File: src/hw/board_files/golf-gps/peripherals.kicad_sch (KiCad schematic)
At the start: 15 parts, among them J2 Micro_SD_Card, U1 NEO-M9N

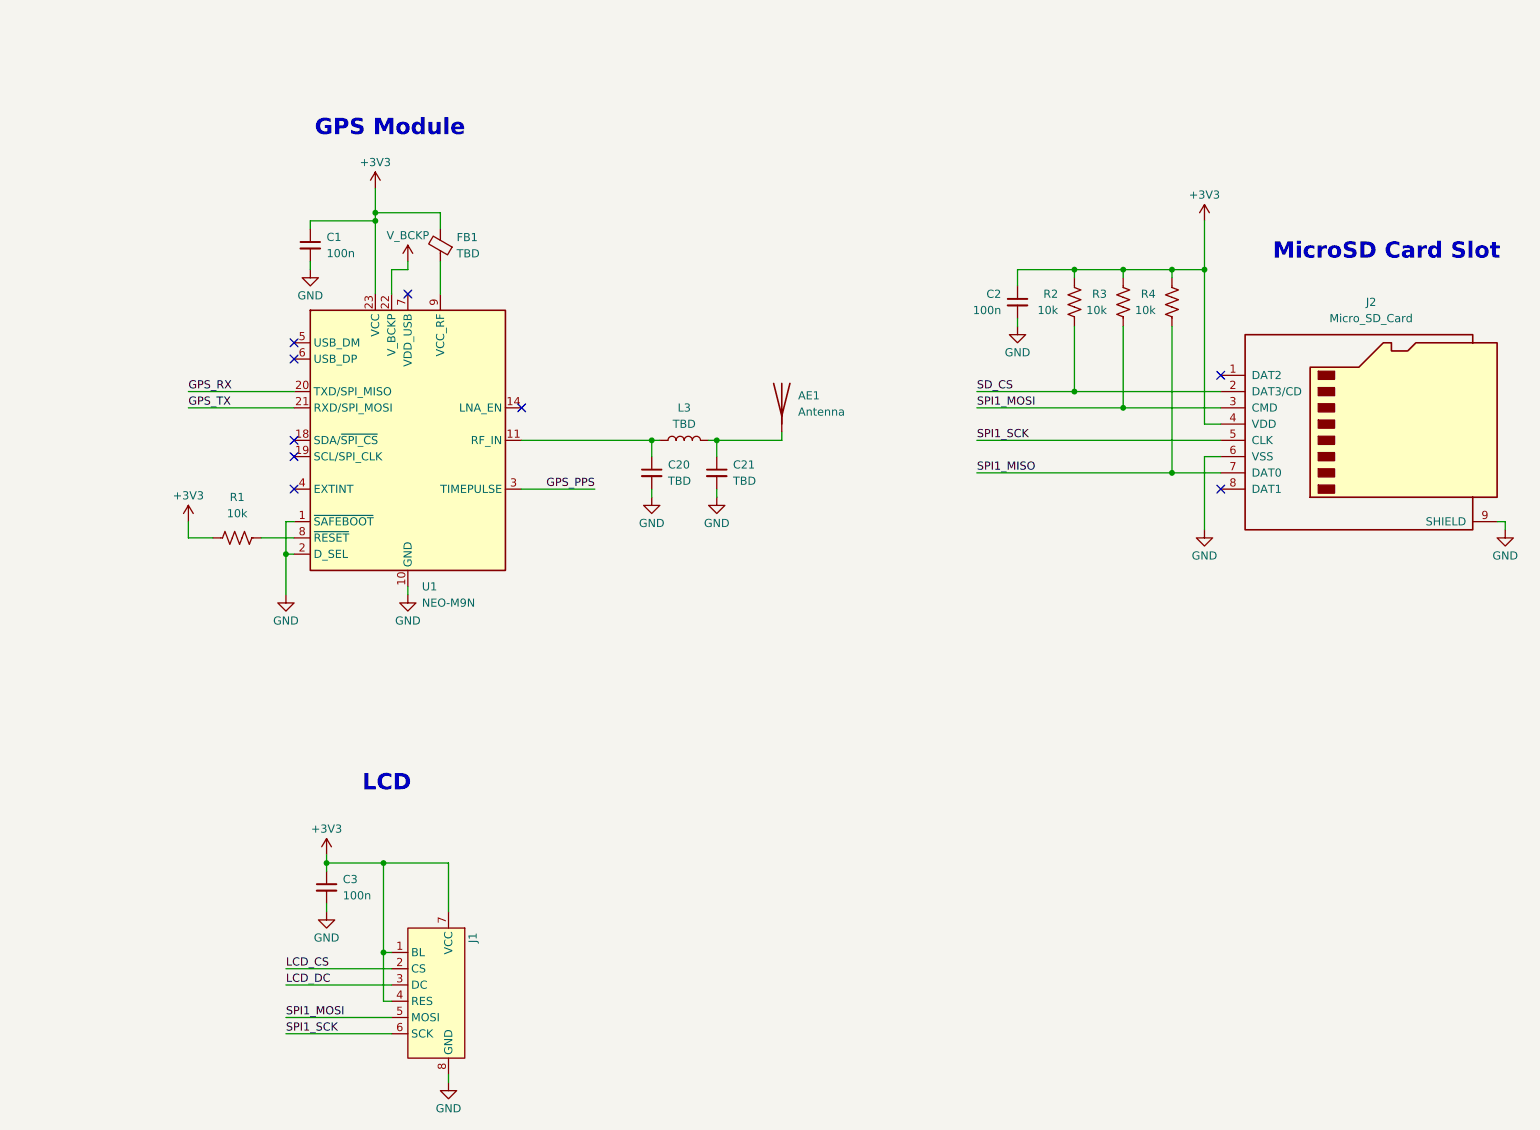
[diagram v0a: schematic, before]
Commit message: Finished sch, started power section on PCB
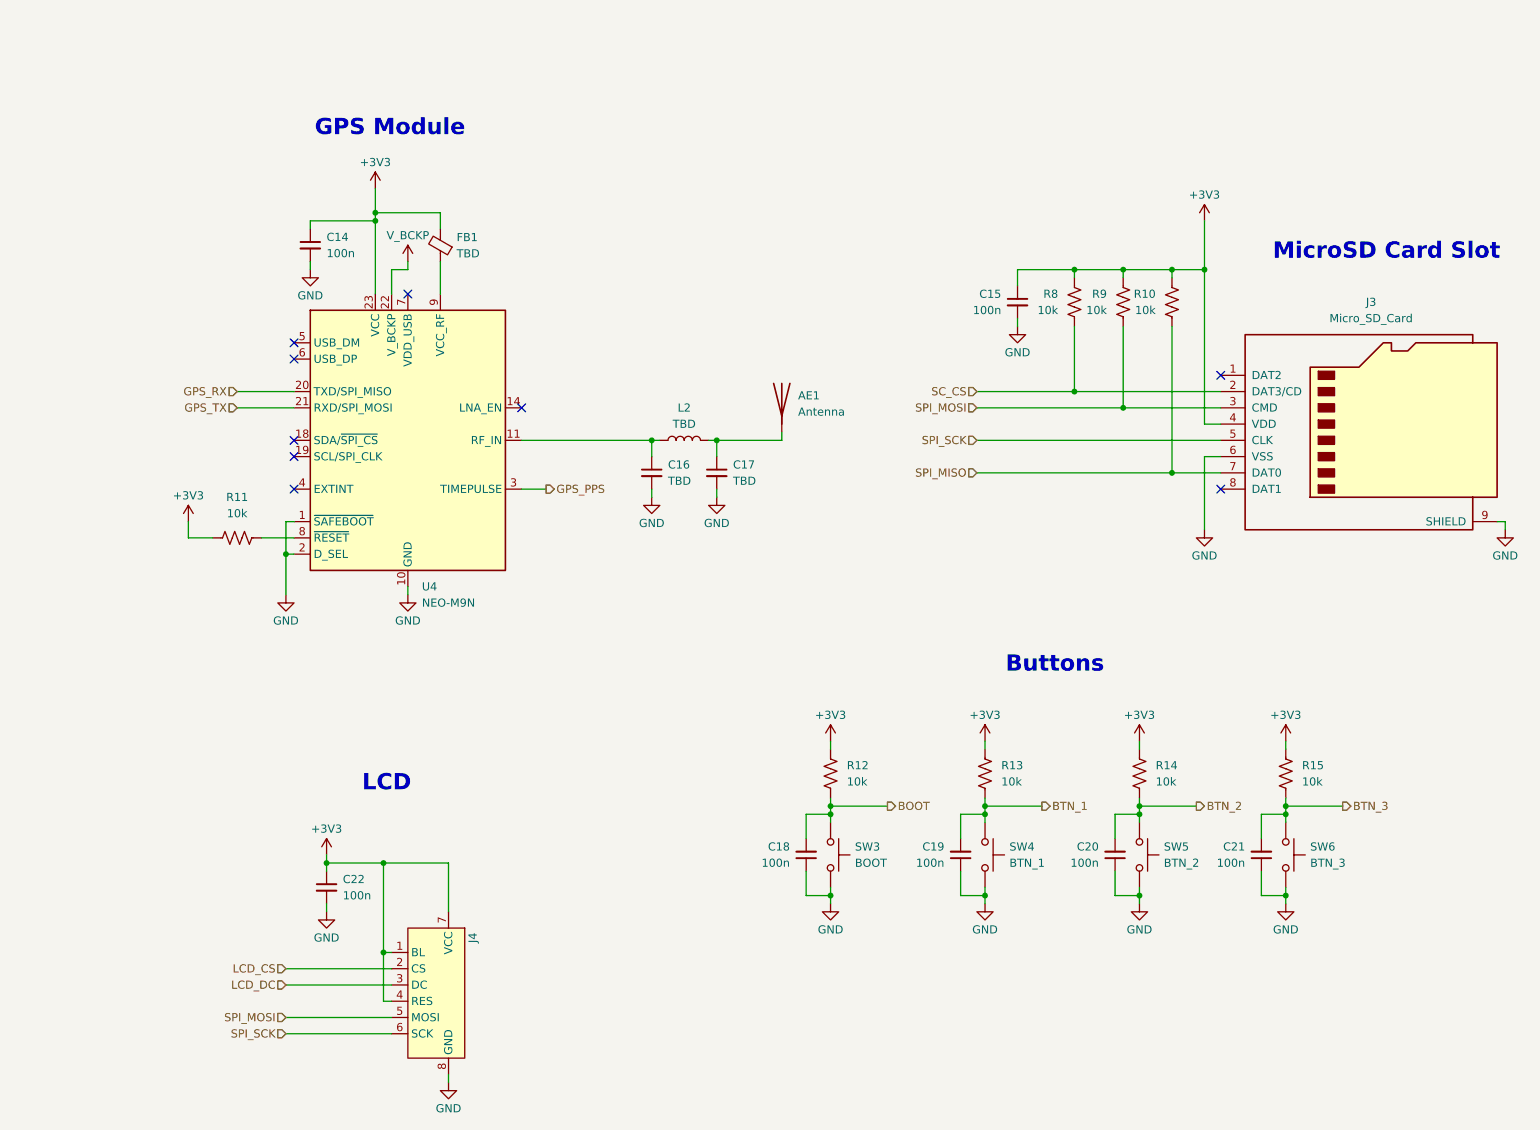
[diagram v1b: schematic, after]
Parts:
- added C18, C19, C20, C21: 100n, Capacitor_SMD:C_0603_1608Metric, symbol Device:C_Small
- added R12, R13, R14, R15: 10k, Resistor_SMD:R_0603_1608Metric, symbol Device:R_US
- added SW3: BOOT, Button_Switch_THT:SW_PUSH_6mm_H4.3mm, symbol Switch:SW_Push
- added SW4: BTN_1, Button_Switch_THT:SW_PUSH_6mm_H4.3mm, symbol Switch:SW_Push
- added SW5: BTN_2, Button_Switch_THT:SW_PUSH_6mm_H4.3mm, symbol Switch:SW_Push
- added SW6: BTN_3, Button_Switch_THT:SW_PUSH_6mm_H4.3mm, symbol Switch:SW_Push
- AE1: footprint (none) -> Library:ANT_GNSSCP-SM12L1_SMD
- C14: renamed from C1; footprint (none) -> Capacitor_SMD:C_0603_1608Metric
- C15: renamed from C2; footprint (none) -> Capacitor_SMD:C_0603_1608Metric
- C16: renamed from C20; footprint (none) -> Capacitor_SMD:C_0603_1608Metric
- C17: renamed from C21; footprint (none) -> Capacitor_SMD:C_0603_1608Metric
- C22: renamed from C3; footprint (none) -> Capacitor_SMD:C_0603_1608Metric
- FB1: footprint (none) -> Inductor_SMD:L_0603_1608Metric
- J3: renamed from J2; footprint (none) -> Connector_Card:microSD_HC_Molex_47219-2001
- L2: renamed from L3; footprint (none) -> Inductor_SMD:L_0603_1608Metric
- R10: renamed from R4; footprint (none) -> Resistor_SMD:R_0603_1608Metric
- R11: renamed from R1; footprint (none) -> Resistor_SMD:R_0603_1608Metric
- R8: renamed from R2; footprint (none) -> Resistor_SMD:R_0603_1608Metric
- R9: renamed from R3; footprint (none) -> Resistor_SMD:R_0603_1608Metric
- renumbered J1 to J4, U1 to U4
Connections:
- net +3V3: now also R12.1, R13.2, R14.2, R15.2
- net GND: now also C18.1, C19.1, C20.1, C21.1, SW3.2, SW4.2, SW5.2, SW6.2
- net SD_CS renamed SC_CS
- net SPI1_MISO renamed SPI_MISO
- net SPI1_MOSI renamed SPI_MOSI
- net SPI1_SCK renamed SPI_SCK
- new net BOOT: C18.2, R12.2, SW3.1
- new net BTN_1: C19.2, R13.1, SW4.1
- new net BTN_2: C20.2, R14.1, SW5.1
- new net BTN_3: C21.2, R15.1, SW6.1
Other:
- note added: "Buttons"
- company: Brady Kuhn -> B. Kuhn

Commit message: PCB Progress
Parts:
- J3: footprint Connector_Card:microSD_HC_Molex_47219-2001 -> Connector_Card:microSD_HC_Wuerth_693072010801
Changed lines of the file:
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@@
 			)
 		)
-		(property "Footprint" "Connector_Card:microSD_HC_Molex_47219-2001"
+		(property "Footprint" "Connector_Card:microSD_HC_Wuerth_693072010801"
 			(at 255.27 69.85 0)
 			(effects

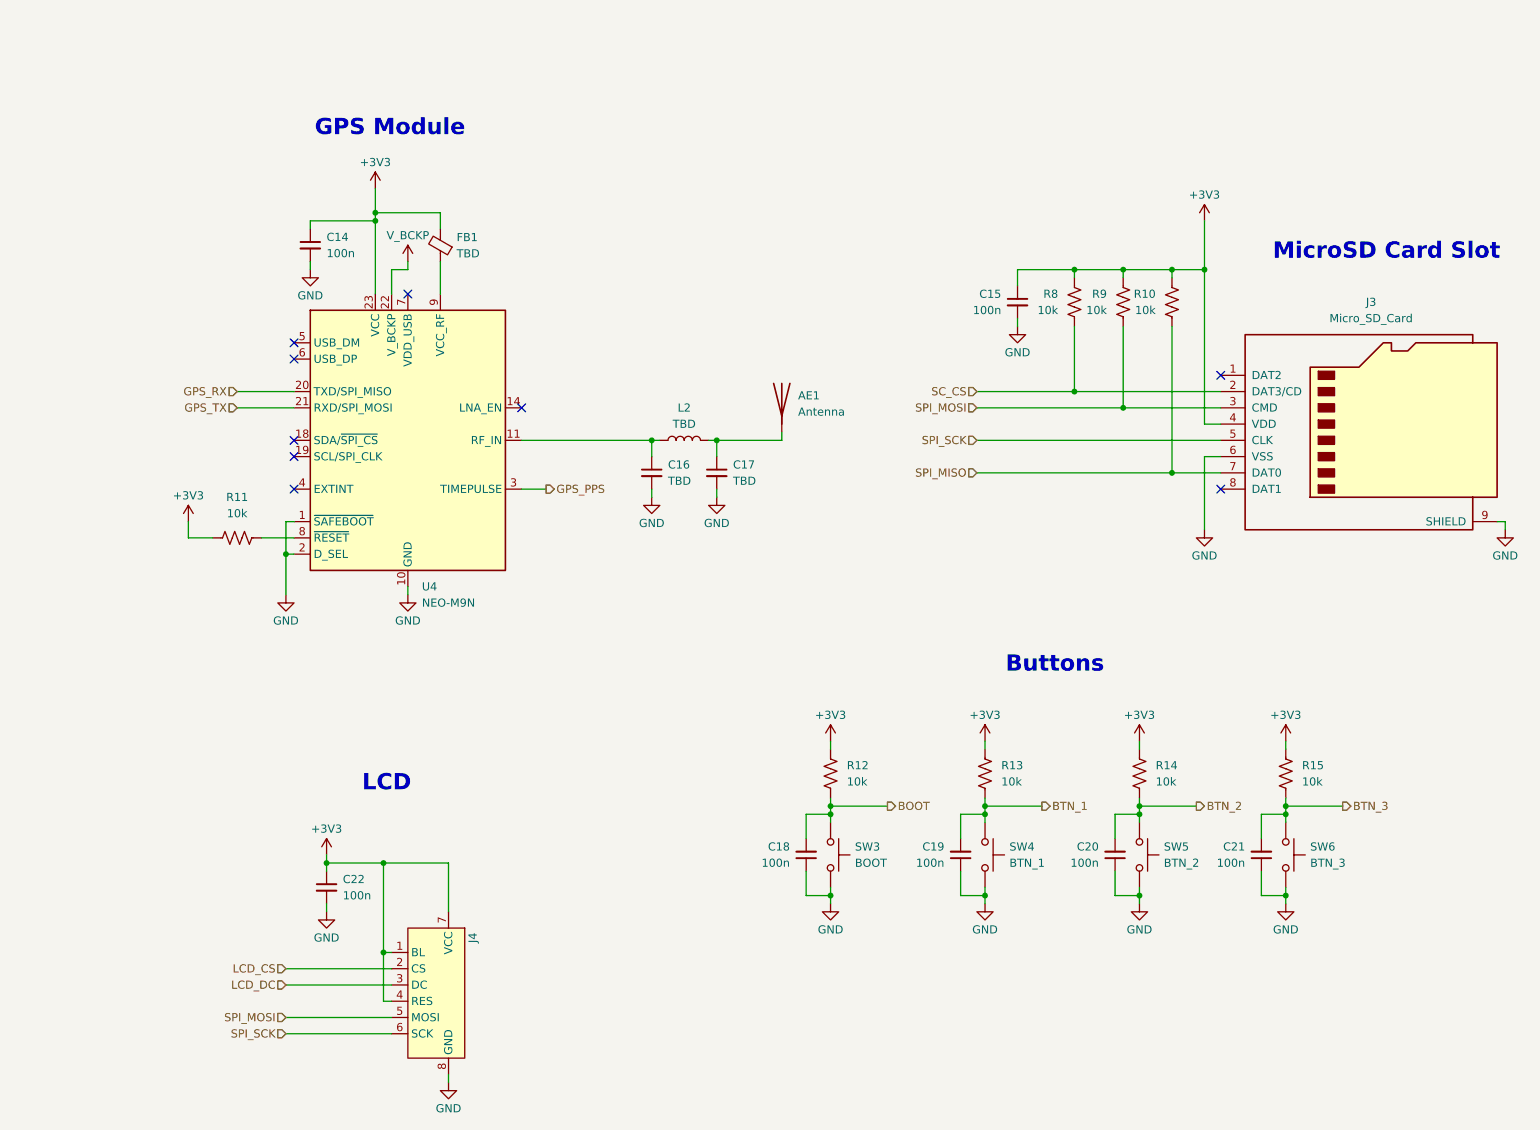
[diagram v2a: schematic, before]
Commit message: Finished new sch. Updated pinout. Started new PCB.
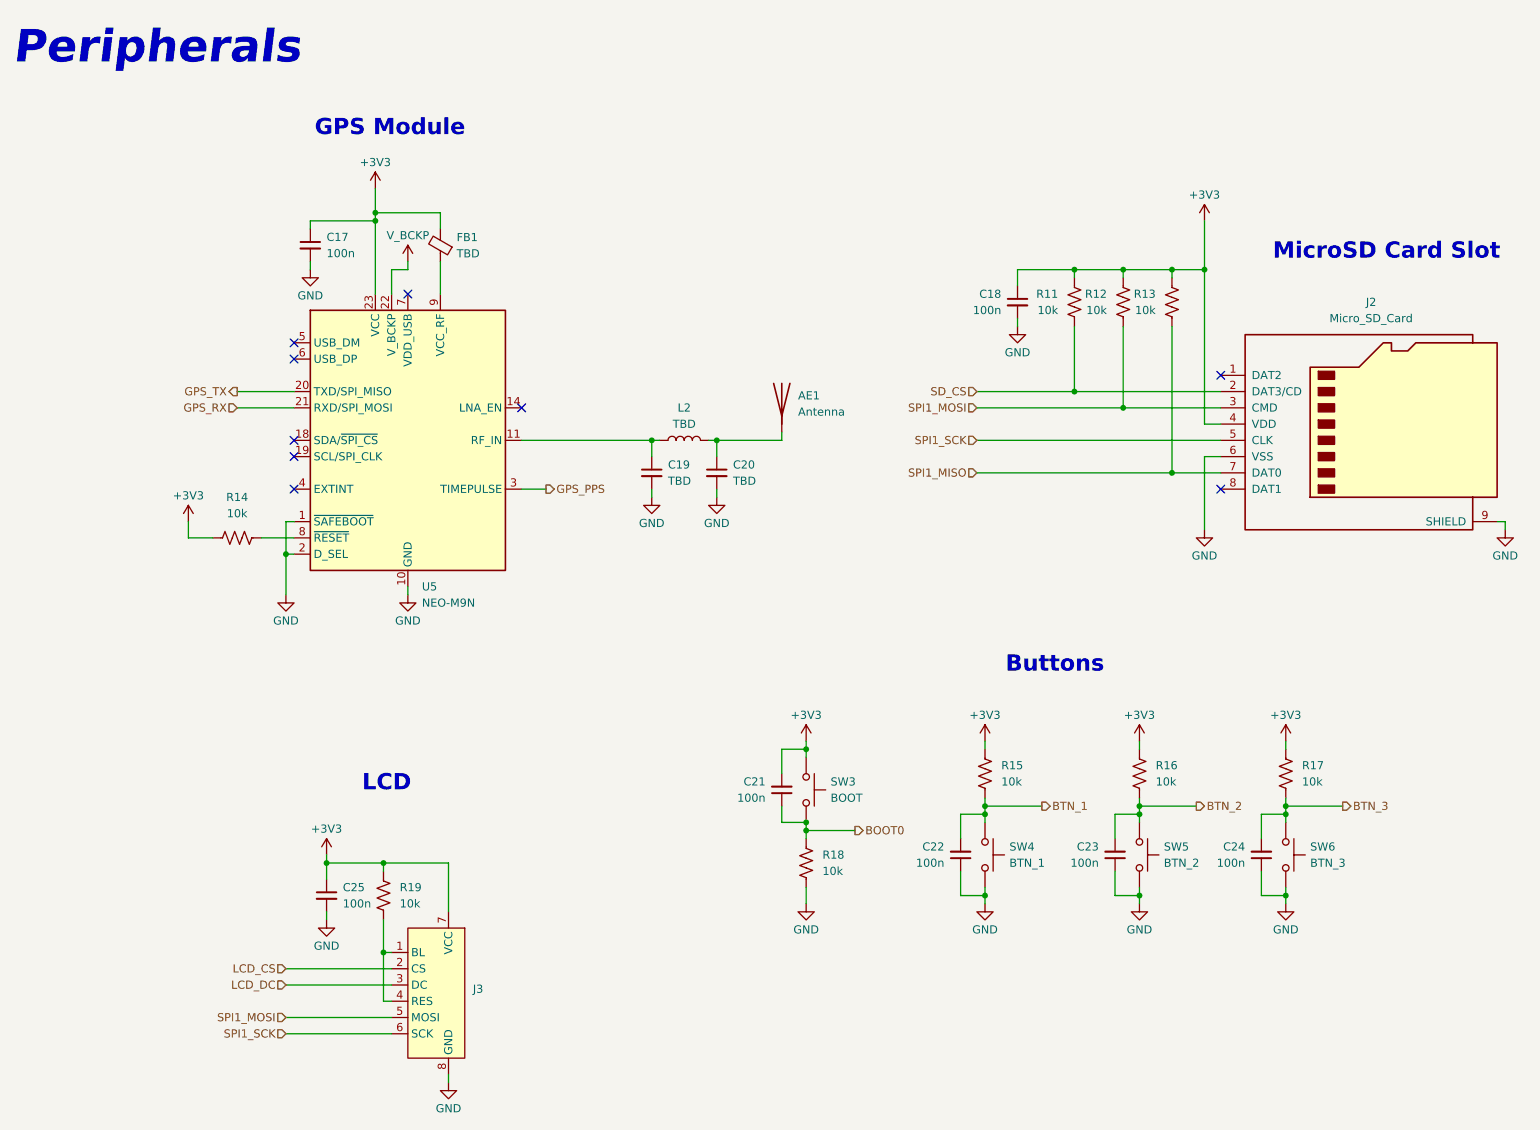
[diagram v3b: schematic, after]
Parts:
- added R19: 10k, Resistor_SMD:R_0603_1608Metric, symbol Device:R_US
- renumbered C14 to C17, C15 to C18, C16 to C19, C17 to C20, C18 to C21, C19 to C22, C20 to C23, C21 to C24, C22 to C25, J3 to J2, J4 to J3, R8 to R11, R9 to R12, R10 to R13, R11 to R14, R13 to R15, R14 to R16, R15 to R17, R12 to R18, U4 to U5
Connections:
- net +3V3: now also C21.2, SW3.1, R19.1; no longer J3.1 (BL), J3.4 (RES), R18.1
- net GND: now also R18.2; no longer C21.1, SW3.2
- net GPS_RX: now also U5.21 (RXD/SPI_MOSI); no longer U5.20 (TXD/SPI_MISO)
- net GPS_TX: now also U5.20 (TXD/SPI_MISO); no longer U5.21 (RXD/SPI_MOSI)
- removed net BOOT: C21.2, R18.2, SW3.1
- net SC_CS renamed SD_CS
- net SPI_MISO renamed SPI1_MISO
- net SPI_MOSI renamed SPI1_MOSI
- net SPI_SCK renamed SPI1_SCK
- new net: J3.1 (BL), J3.4 (RES), R19.2
- new net BOOT0: C21.1, R18.1, SW3.2
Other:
- note added: "Peripherals"
- moved on the sheet: C21, C25, R18, SW3

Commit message: Removed USB to UART bridge, added VDDA decoupling, adjusted MCU pinout and updated spreadsheet
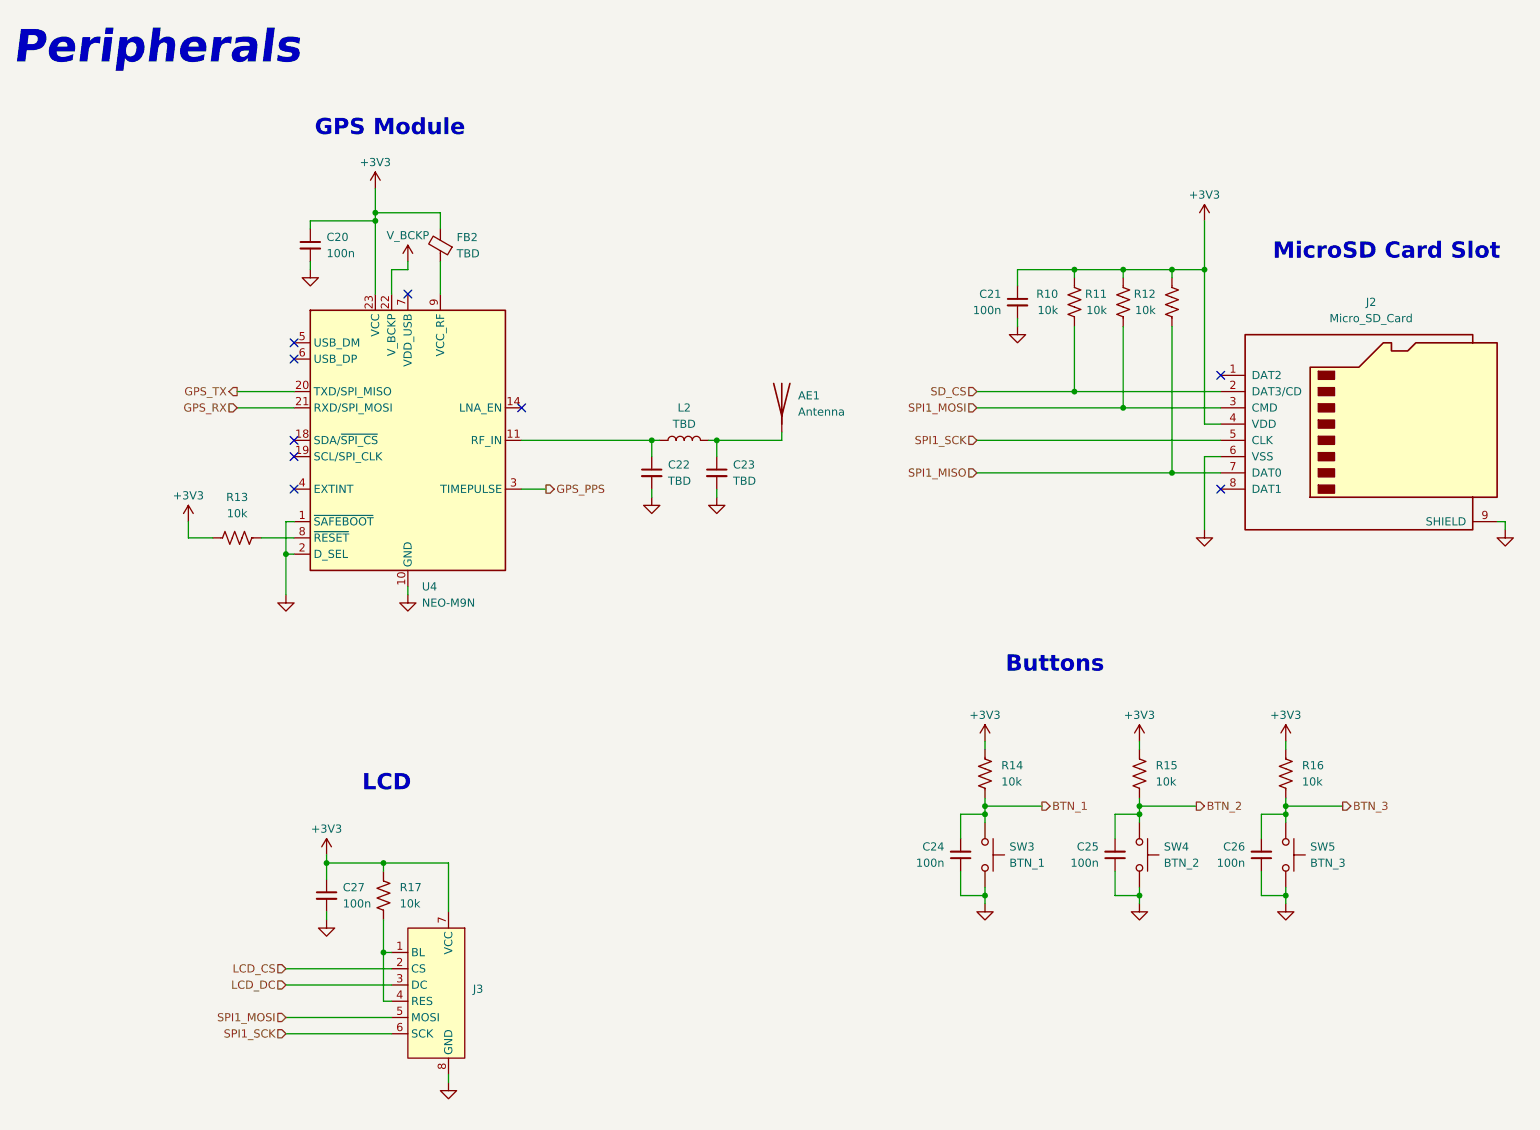
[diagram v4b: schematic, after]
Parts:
- removed C21: 100n, Capacitor_SMD:C_0603_1608Metric, symbol Device:C_Small
- removed R18: 10k, Resistor_SMD:R_0603_1608Metric, symbol Device:R_US
- removed SW3: BOOT, Button_Switch_THT:SW_PUSH_6mm_H4.3mm, symbol Switch:SW_Push
- renumbered C17 to C20, C18 to C21, C19 to C22, C20 to C23, C22 to C24, C23 to C25, C24 to C26, C25 to C27, FB1 to FB2, R11 to R10, R12 to R11, R13 to R12, R14 to R13, R15 to R14, R16 to R15, R17 to R16, R19 to R17, SW4 to SW3, SW5 to SW4, SW6 to SW5, U5 to U4
